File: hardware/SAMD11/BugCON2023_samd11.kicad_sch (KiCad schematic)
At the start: 52 parts, among them J1 I2C, J5 Serial, P1 USB_C_Plug_USB2.0, Q1 DMG3415U-7, SW1 RESET, SW2 ON, SW3 SW_Push, SW4 SW_Push, U1 W25Q16JV, U2 AP2112K-3.3, U3 RP2040, Y1 12MHz

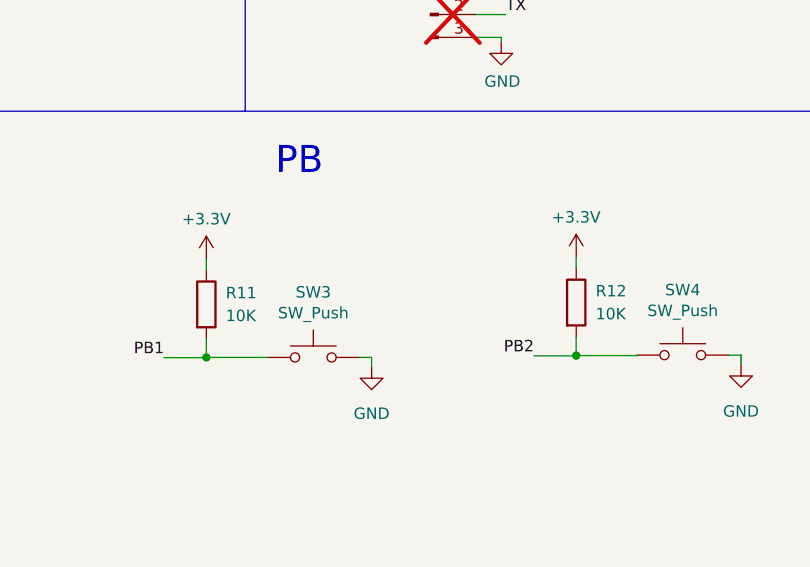
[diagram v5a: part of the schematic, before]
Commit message: change buttons to the front and remove pull up resistors
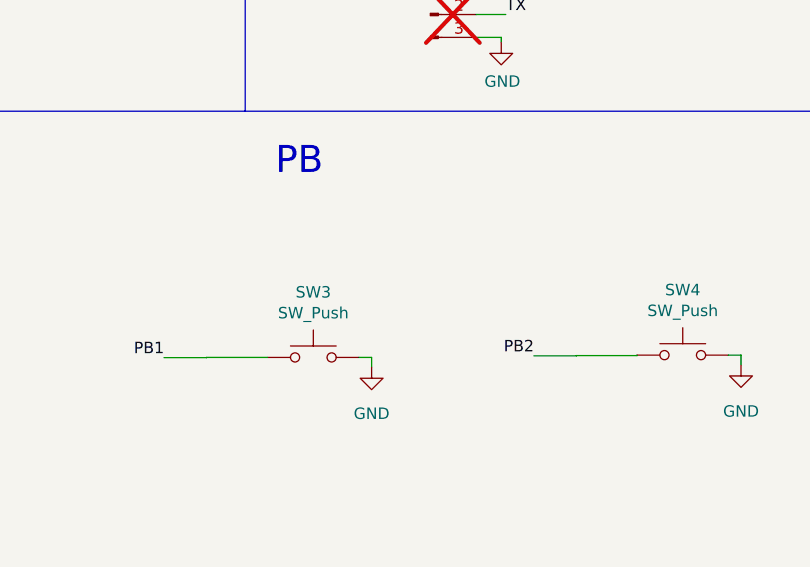
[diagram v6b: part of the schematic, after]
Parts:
- removed R11, R12: 10K, Resistor_SMD:R_0603_1608Metric, symbol Device:R
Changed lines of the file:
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@@
   (junction (at 50.7492 108.204) (diameter 0) (color 0 0 0 0)
   )
-  (junction (at 191.897 102.9208) (diameter 0) (color 0 0 0 0)
-  )
   (junction (at 307.975 122.682) (diameter 0) (color 0 0 0 0)
   )
@@
   (junction (at 90.805 46.355) (diameter 0) (color 0 0 0 0)
   )
-  (junction (at 232.9942 102.7176) (diameter 0) (color 0 0 0 0)
-  )
   (junction (at 254.8636 41.3258) (diameter 0) (color 0 0 0 0)
   )
@@
     (stroke (width 0) (type default))
   )
-  (wire (pts (xy 191.897 100.838) (xy 191.897 102.9208))
-    (stroke (width 0) (type default))
-  )
   (wire (pts (xy 24.511 157.734) (xy 27.051 157.734))
     (stroke (width 0) (type default))
@@
     (stroke (width 0) (type default))
   )
-  (wire (pts (xy 191.897 91.9988) (xy 191.897 93.218))
-    (stroke (width 0) (type default))
-  )
   (polyline (pts (xy 196.215 75.565) (xy 284.48 75.565))
     (stroke (width 0) (type default))
@@
     (stroke (width 0) (type default))
   )
-  (wire (pts (xy 232.9942 91.7956) (xy 232.9942 93.0148))
-    (stroke (width 0) (type default))
-  )
   (polyline (pts (xy 77.47 75.565) (xy 86.995 75.565))
     (stroke (width 0) (type default))
@@
     (stroke (width 0) (type default))
   )
-  (wire (pts (xy 232.9942 100.6348) (xy 232.9942 102.7176))
-    (stroke (width 0) (type default))
-  )
   (wire (pts (xy 42.545 37.465) (xy 44.323 37.465))
     (stroke (width 0) (type default))
@@
     )
   )
-  (symbol (lib_id "Device:R") (at 232.9942 96.8248 0) (unit 1)
-    (in_bom yes) (on_board yes) (dnp no) (fields_autoplaced)
-    (property "Reference" "R12" (at 235.1532 95.5548 0)
-      (effects (font (size 1.27 1.27)) (justify left))
-    )
-    (property "Value" "10K" (at 235.1532 98.0948 0)
-      (effects (font (size 1.27 1.27)) (justify left))
-    )
-    (property "Footprint" "Resistor_SMD:R_0603_1608Metric" (at 231.2162 96.8248 90)
-      (effects (font (size 1.27 1.27)) hide)
-    )
-    (property "Datasheet" "~" (at 232.9942 96.8248 0)
-      (effects (font (size 1.27 1.27)) hide)
-    )
-    (property "LCSC#" "C98220" (at 232.9942 96.8248 0)
-      (effects (font (size 1.27 1.27)) hide)
-    )
-    (property "Proveedor" "LCSC" (at 232.9942 96.8248 0)
-      (effects (font (size 1.27 1.27)) hide)
-    )
-    (property "manf#" "RC0603FR-0710KL" (at 232.9942 96.8248 0)
-      (effects (font (size 1.27 1.27)) hide)
-    )
-    (pin "1")
-    (pin "2")
-    (instances
-      (project "BugCON2023_samd11"
-        (path "/3412b91a-b939-4a2e-ae82-c762ad3cc219"
-          (reference "R12") (unit 1)
-        )
-      )
-    )
-  )
   (symbol (lib_id "Device:Battery_Cell") (at 175.895 47.625 0) (unit 1)
     (in_bom yes) (on_board yes) (dnp no) (fields_autoplaced)
@@
     )
   )
-  (symbol (lib_id "Device:R") (at 191.897 97.028 0) (unit 1)
-    (in_bom yes) (on_board yes) (dnp no) (fields_autoplaced)
-    (property "Reference" "R11" (at 194.056 95.758 0)
-      (effects (font (size 1.27 1.27)) (justify left))
-    )
-    (property "Value" "10K" (at 194.056 98.298 0)
-      (effects (font (size 1.27 1.27)) (justify left))
-    )
-    (property "Footprint" "Resistor_SMD:R_0603_1608Metric" (at 190.119 97.028 90)
-      (effects (font (size 1.27 1.27)) hide)
-    )
-    (property "Datasheet" "~" (at 191.897 97.028 0)
-      (effects (font (size 1.27 1.27)) hide)
-    )
-    (property "LCSC#" "C98220" (at 191.897 97.028 0)
-      (effects (font (size 1.27 1.27)) hide)
-    )
-    (property "Proveedor" "LCSC" (at 191.897 97.028 0)
-      (effects (font (size 1.27 1.27)) hide)
-    )
-    (property "manf#" "RC0603FR-0710KL" (at 191.897 97.028 0)
-      (effects (font (size 1.27 1.27)) hide)
-    )
-    (pin "1")
-    (pin "2")
-    (instances
-      (project "BugCON2023_samd11"
-        (path "/3412b91a-b939-4a2e-ae82-c762ad3cc219"
-          (reference "R11") (unit 1)
-        )
-      )
-    )
-  )
   (symbol (lib_id "Device:C_Small") (at 89.281 202.184 0) (unit 1)
     (in_bom yes) (on_board yes) (dnp no) (fields_autoplaced)
@@
     )
   )
-  (symbol (lib_id "power:+3.3V") (at 232.9942 91.7956 0) (unit 1)
-    (in_bom yes) (on_board yes) (dnp no) (fields_autoplaced)
-    (property "Reference" "#PWR069" (at 232.9942 95.6056 0)
-      (effects (font (size 1.27 1.27)) hide)
-    )
-    (property "Value" "+3.3V" (at 232.9942 87.3506 0)
-      (effects (font (size 1.27 1.27)))
-    )
-    (property "Footprint" "" (at 232.9942 91.7956 0)
-      (effects (font (size 1.27 1.27)) hide)
-    )
-    (property "Datasheet" "" (at 232.9942 91.7956 0)
-      (effects (font (size 1.27 1.27)) hide)
-    )
-    (pin "1")
-    (instances
-      (project "BugCON2023_samd11"
-        (path "/3412b91a-b939-4a2e-ae82-c762ad3cc219"
-          (reference "#PWR069") (unit 1)
-        )
-      )
-    )
-  )
   (symbol (lib_id "power:GND") (at 226.822 43.9928 0) (unit 1)
     (in_bom yes) (on_board yes) (dnp no) (fields_autoplaced)
@@
         )
       )
-    )
-  )
-  (symbol (lib_id "power:+3.3V") (at 191.897 91.9988 0) (unit 1)
-    (in_bom yes) (on_board yes) (dnp no) (fields_autoplaced)
-    (property "Reference" "#PWR067" (at 191.897 95.8088 0)
-      (effects (font (size 1.27 1.27)) hide)
-    )
-    (property "Value" "+3.3V" (at 191.897 87.5538 0)
-      (effects (font (size 1.27 1.27)))
-    )
-    (property "Footprint" "" (at 191.897 91.9988 0)
-      (effects (font (size 1.27 1.27)) hide)
-    )
-    (property "Datasheet" "" (at 191.897 91.9988 0)
-      (effects (font (size 1.27 1.27)) hide)
-    )
-    (pin "1")
-    (instances
-      (project "BugCON2023_samd11"
-        (path "/3412b91a-b939-4a2e-ae82-c762ad3cc219"
-          (reference "#PWR067") (unit 1)
-        )
-      )

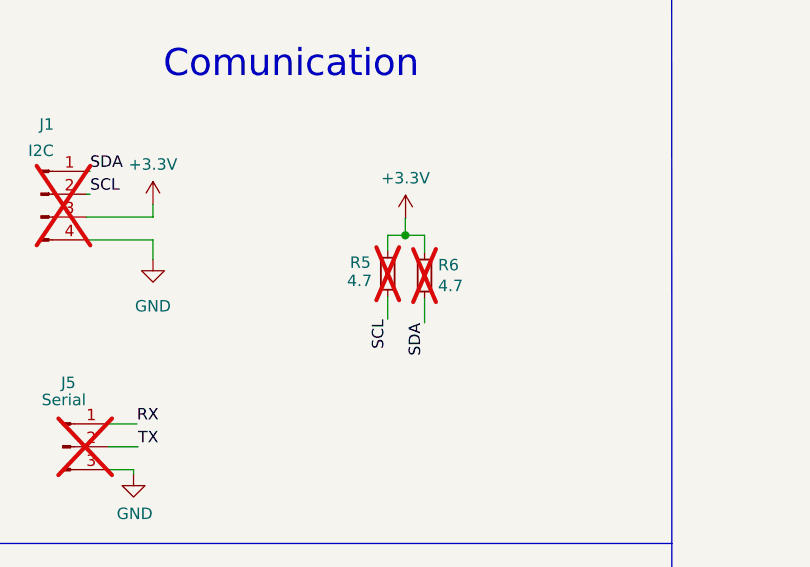
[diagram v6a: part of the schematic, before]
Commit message: Rename_Pullup´s
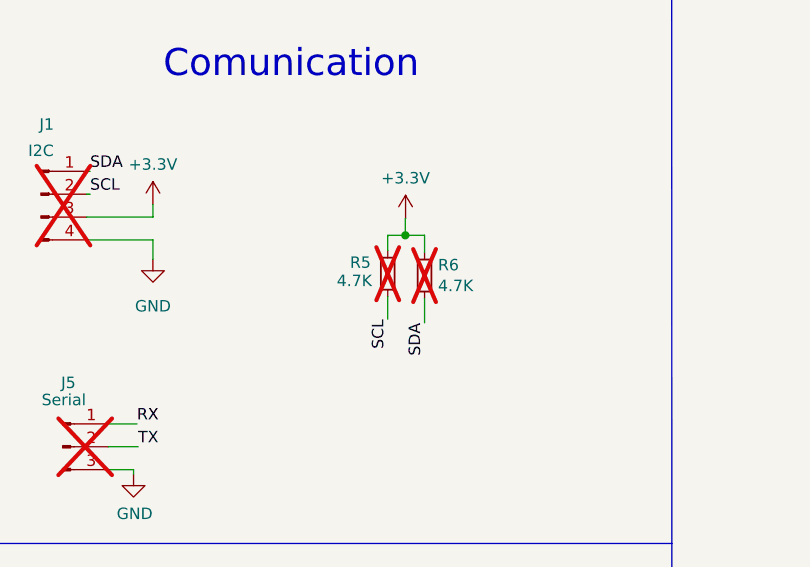
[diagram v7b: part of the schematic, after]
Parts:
- R5, R6: value 4.7 -> 4.7K
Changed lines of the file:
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@@
       (effects (font (size 1.27 1.27)) (justify left))
     )
-    (property "Value" "4.7" (at 251.1552 46.3804 0)
+    (property "Value" "4.7K" (at 251.1552 46.3804 0)
       (effects (font (size 1.27 1.27)) (justify left))
     )
@@
       (effects (font (size 1.27 1.27)) hide)
     )
-    (property "Datasheet" "http://www.onsemi.com/pub_link/Collateral/MBR340-D.PDF" (at 129.667 52.705 0)
+    (property "Datasheet" "" (at 129.667 52.705 0)
       (effects (font (size 1.27 1.27)) hide)
     )
@@
       (effects (font (size 1.27 1.27)) (justify left))
     )
-    (property "Value" "4.7" (at 258.4958 46.9392 0)
+    (property "Value" "4.7K" (at 258.4958 46.9392 0)
       (effects (font (size 1.27 1.27)) (justify left))
     )
